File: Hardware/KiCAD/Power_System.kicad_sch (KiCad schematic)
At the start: 5 parts, among them IC5 ISL91127IRNZ-T7A, IC7 TPS61235PRWLT, IC8 BQ24193RGER, U2 BQ297xy

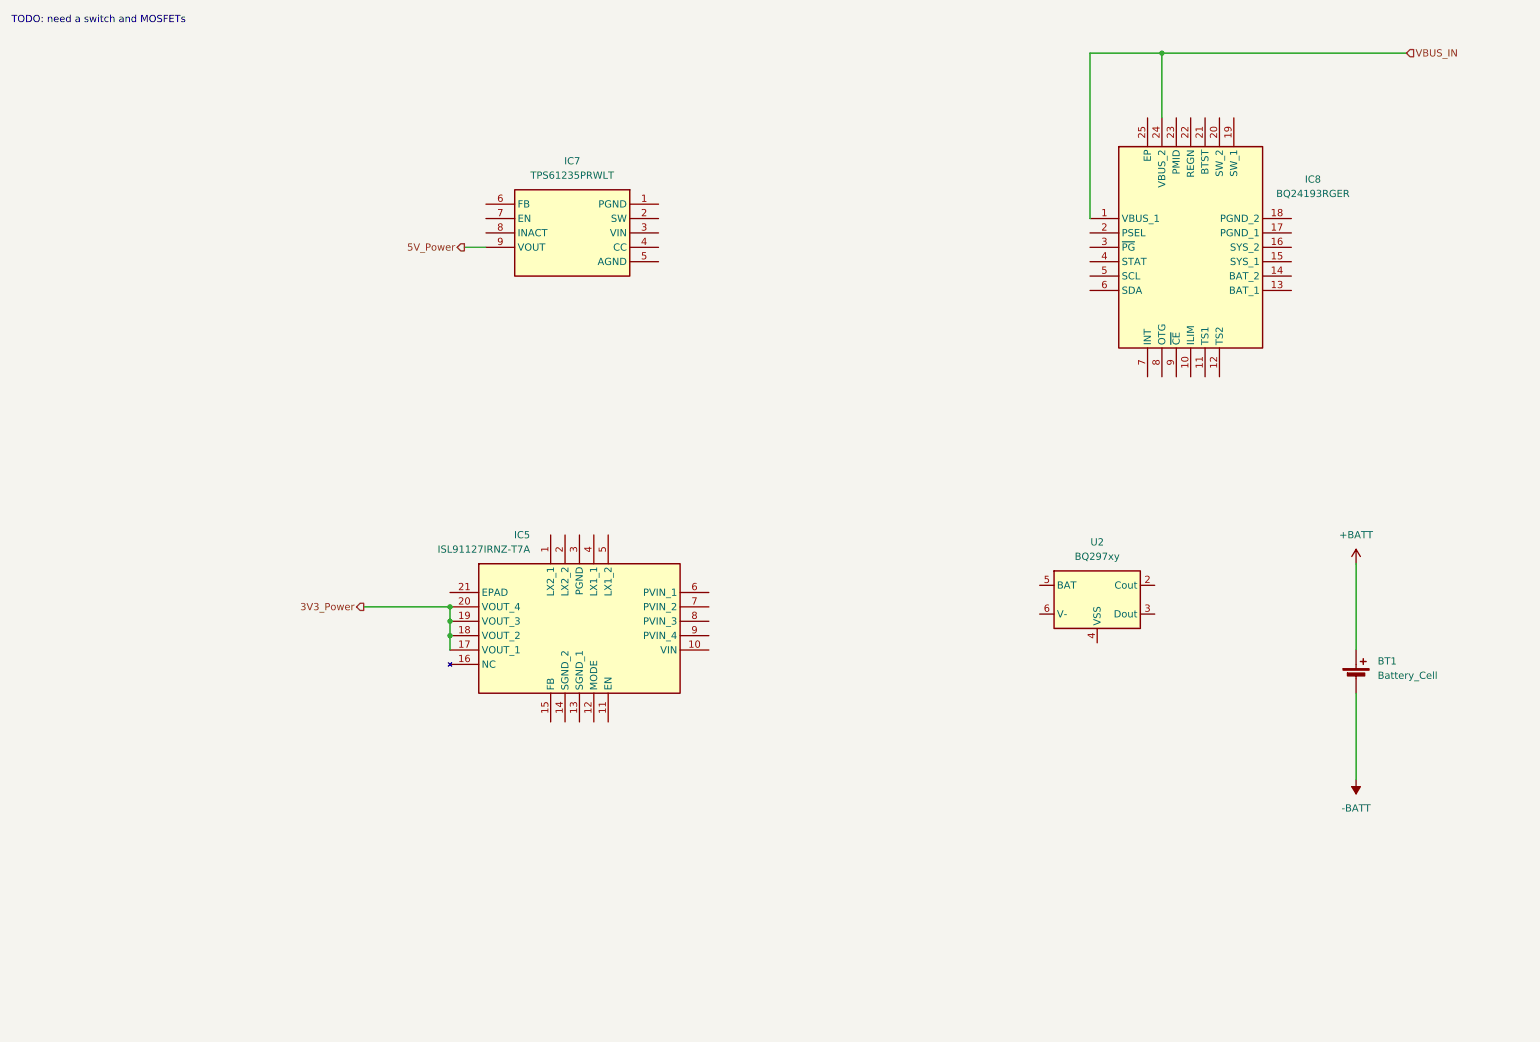
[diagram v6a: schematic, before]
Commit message: feat: subsystem exploration, begin placement, routing #11 #12 #4 many new project symbols
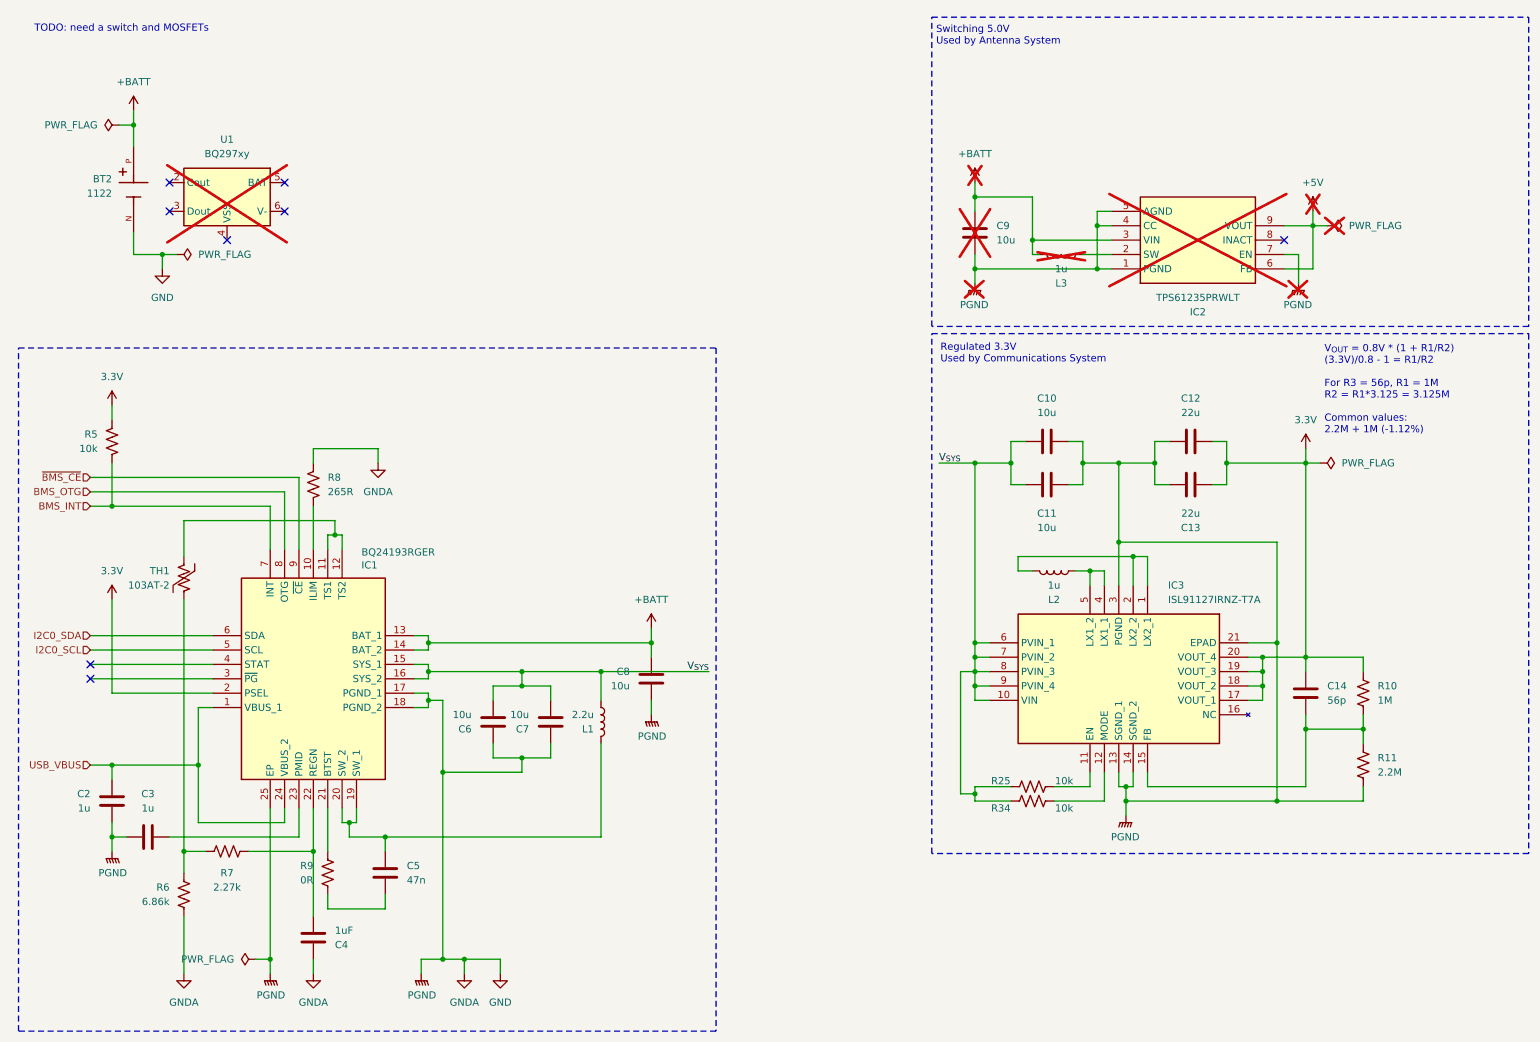
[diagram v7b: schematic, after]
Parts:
- removed BT1: Battery_Cell, symbol Device:Battery_Cell
- added BT2: 1122, Cobalt_Cowboy:BAT_1122, symbol Cobalt-Cowboy:1122
- added C10, C11, C6, C7, C8, C9: 10u, Capacitor_SMD:C_0603_1608Metric_Pad1.08x0.95mm_HandSolder, symbol Device:C
- added C12, C13: 22u, Capacitor_SMD:C_0603_1608Metric_Pad1.08x0.95mm_HandSolder, symbol Device:C
- added C14: 56p, Capacitor_SMD:C_0603_1608Metric_Pad1.08x0.95mm_HandSolder, symbol Device:C
- added C2, C3: 1u, Capacitor_SMD:C_0603_1608Metric_Pad1.08x0.95mm_HandSolder, symbol Device:C
- added C4: 1uF, Capacitor_SMD:C_0603_1608Metric_Pad1.08x0.95mm_HandSolder, symbol Device:C
- added C5: 47n, Capacitor_SMD:C_0603_1608Metric_Pad1.08x0.95mm_HandSolder, symbol Device:C
- added L1: 2.2u, Inductor_SMD:L_Coilcraft_XxL4020, symbol Device:L
- added L2: 1u, Inductor_SMD:L_Coilcraft_XxL4020, symbol Device:L
- added L3: 1u, Inductor_SMD:L_0603_1608Metric, symbol Device:L
- added R10: 1M, Resistor_SMD:R_0603_1608Metric, symbol Device:R_US
- added R11: 2.2M, Resistor_SMD:R_0603_1608Metric, symbol Device:R_US
- added R25, R34, R5: 10k, Resistor_SMD:R_0603_1608Metric, symbol Device:R_US
- added R6: 6.86k, Resistor_SMD:R_0603_1608Metric, symbol Device:R_US
- added R7: 2.27k, Resistor_SMD:R_0603_1608Metric, symbol Device:R_US
- added R8: 265R, Resistor_SMD:R_0603_1608Metric, symbol Device:R_US
- added R9: 0R, Resistor_SMD:R_0603_1608Metric, symbol Device:R_US
- added TH1: 103AT-2, Cobalt_Cowboy:103AT2, symbol Device:Thermistor_US
- IC2: renamed from IC7; now not fitted
- U1: renamed from U2; now not fitted
- renumbered IC8 to IC1, IC5 to IC3
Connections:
- net 3V3_Power is gone; now on net 3.3V: IC3.17 (VOUT_1), IC3.18 (VOUT_2), IC3.19 (VOUT_3), IC3.20 (VOUT_4)
- net 5V_Power is gone; now on net +5V: IC2.9 (VOUT)
- net +BATT: now also IC1.13 (BAT_1), IC1.14 (BAT_2), IC2.3 (VIN), BT2.P, C8.1, C9.1, L3.2
- net GND: now reaches IC2.1 (PGND)
- net GND: now also IC1.17 (PGND_1), IC1.18 (PGND_2), IC1.25 (EP), IC2.4 (CC), IC2.5 (AGND), IC2.7 (EN), IC3.13 (SGND_1), IC3.14 (SGND_2), IC3.21 (EPAD), IC3.3 (PGND), BT2.N, C10.1, C11.1, C12.2, C13.2, C2.2, C3.2, C4.1, C6.1, C7.1, C8.2, C9.2, R11.2, R6.2, R8.2
- net at IC2.2 (SW): now also L3.1
- net +5V: now reaches IC2.6 (FB)
- net at IC3.1 (LX2_1): now also IC3.2 (LX2_2), L2.2
- net V_{SYS}: now reaches IC3.10 (VIN)
- net V_{SYS}: now also IC1.15 (SYS_1), IC1.16 (SYS_2), IC3.6 (PVIN_1), IC3.7 (PVIN_2), IC3.8 (PVIN_3), IC3.9 (PVIN_4), C10.2, C11.2, C6.2, C7.2, L1.2, R25.1, R34.2
- net at IC3.11 (EN): now also R25.2
- net at IC3.12 (MODE): now also R34.1
- net at IC3.15 (FB): now also C14.2, R10.2, R11.1
- net at IC3.4 (LX1_1): now also IC3.5 (LX1_2), L2.1
- net at IC1.10 (ILIM): now also R8.1
- net at IC1.11 (TS1): now also IC1.12 (TS2), TH1.2
- net at IC1.19 (SW_1): now also IC1.20 (SW_2), C5.2, L1.1
- net 3.3V: now reaches IC1.2 (PSEL)
- net 3.3V: now also C12.1, C13.1, C14.1, R10.1, R5.1
- net at IC1.21 (BTST): now also R9.2
- net at IC1.22 (REGN): now also C4.2, R7.1
- net at IC1.23 (PMID): now also C3.1
- net I2C0_SCL: now reaches IC1.5 (SCL)
- net I2C0_SDA: now reaches IC1.6 (SDA)
- net BMS_INT: now reaches IC1.7 (INT)
- net BMS_INT: now also R5.2
- net BMS_OTG: now reaches IC1.8 (OTG)
- net ~{BMS_CE}: now reaches IC1.9 (~{CE})
- net VBUS_IN renamed USB_VBUS
- net USB_VBUS: now also C2.1
- new net: C5.1, R9.1
- new net: R6.1, R7.2, TH1.1
- no-connect marks 0 -> 8
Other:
- note added: "Regulated 3.3V Used by Communications System"
- note added: "Switching 5.0V Used by Antenna System"
- note added: "V_{OUT} = 0.8V * (1 + R1/R2) (3.3V)/0.8 - 1 = R1/R2 For R3 = 56p, R1 = 1M R2 = R1*3.125 = 3.125M Common values: 2.2M + 1M (-1.12%)"
- moved on the sheet: IC1, IC3

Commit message: feat: Plot updated schematics #11
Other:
- note added: "BMS Single-Cell"
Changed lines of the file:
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@@
+		)
+	)
+	(text "BMS Single-Cell"
+		(exclude_from_sim no)
+		(at 16.256 75.184 0)
+		(effects
+			(font
+				(size 1.27 1.27)
+			)
+			(justify left top)
 		)
 	)
